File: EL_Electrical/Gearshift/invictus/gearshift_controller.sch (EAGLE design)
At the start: 70 parts, among them IC1 MCP2562-E_SN, IC2 MCP2515-I_SO, Q1 BSS138, Q10 BSS138, Q2 BSS138, Q3 BSS138, Q4 BSS138, Q5 BSS138, Q6 BSS138, Q8 BSS138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

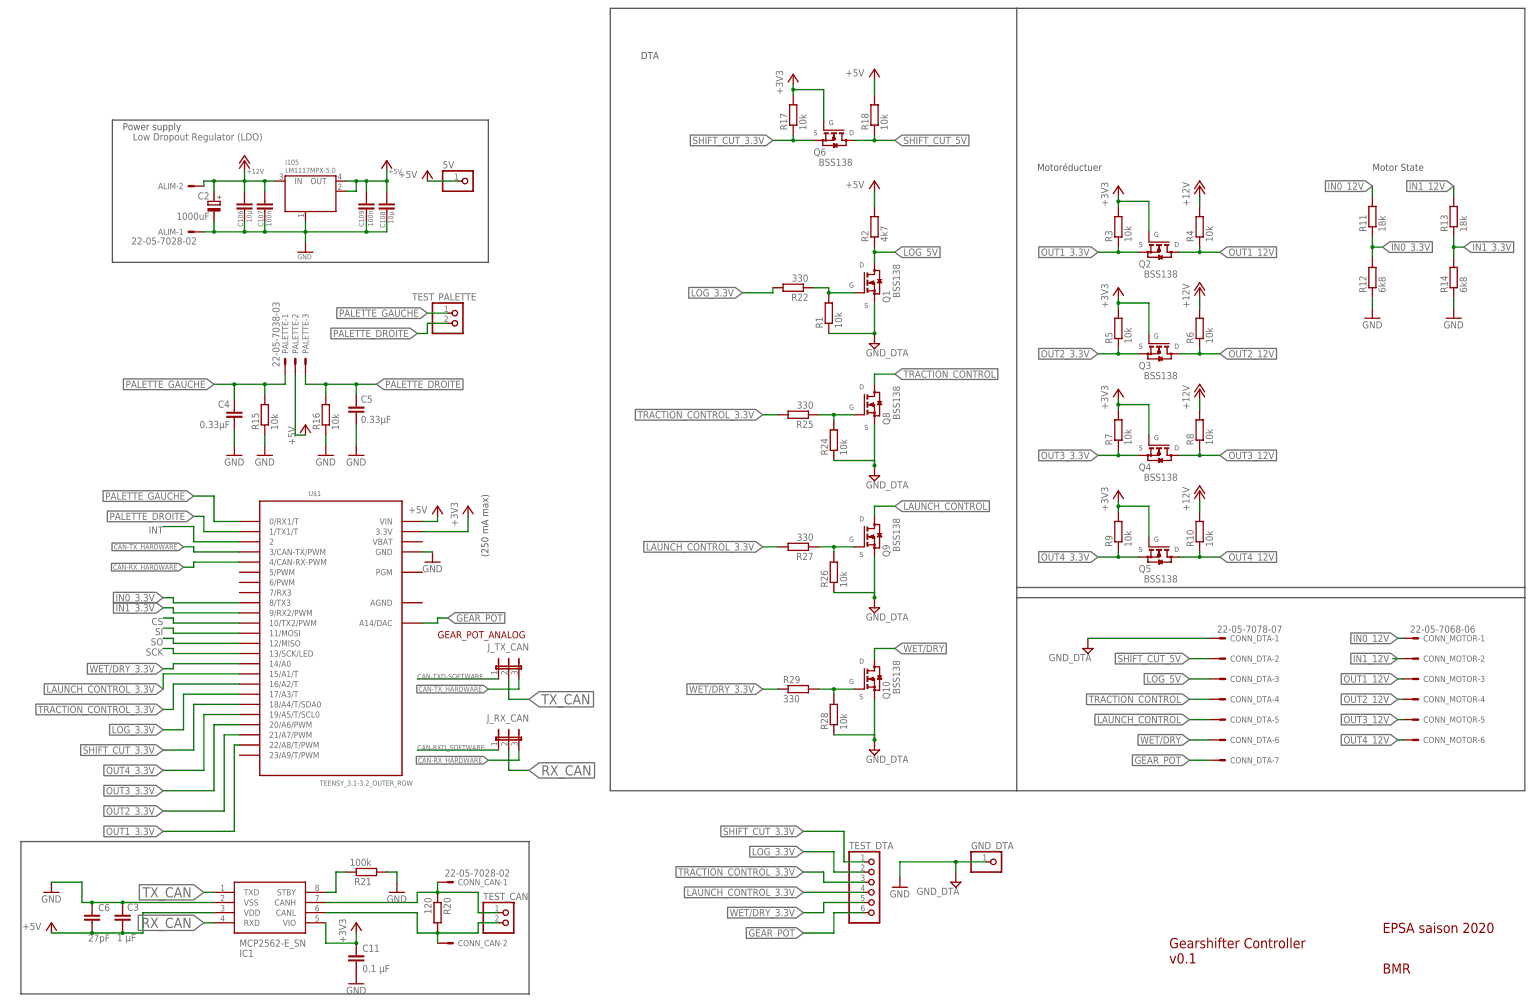
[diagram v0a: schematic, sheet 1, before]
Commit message: Add neutral sensor connector (to use with Teensy's pull-up resistors), delete uselless dta test pins
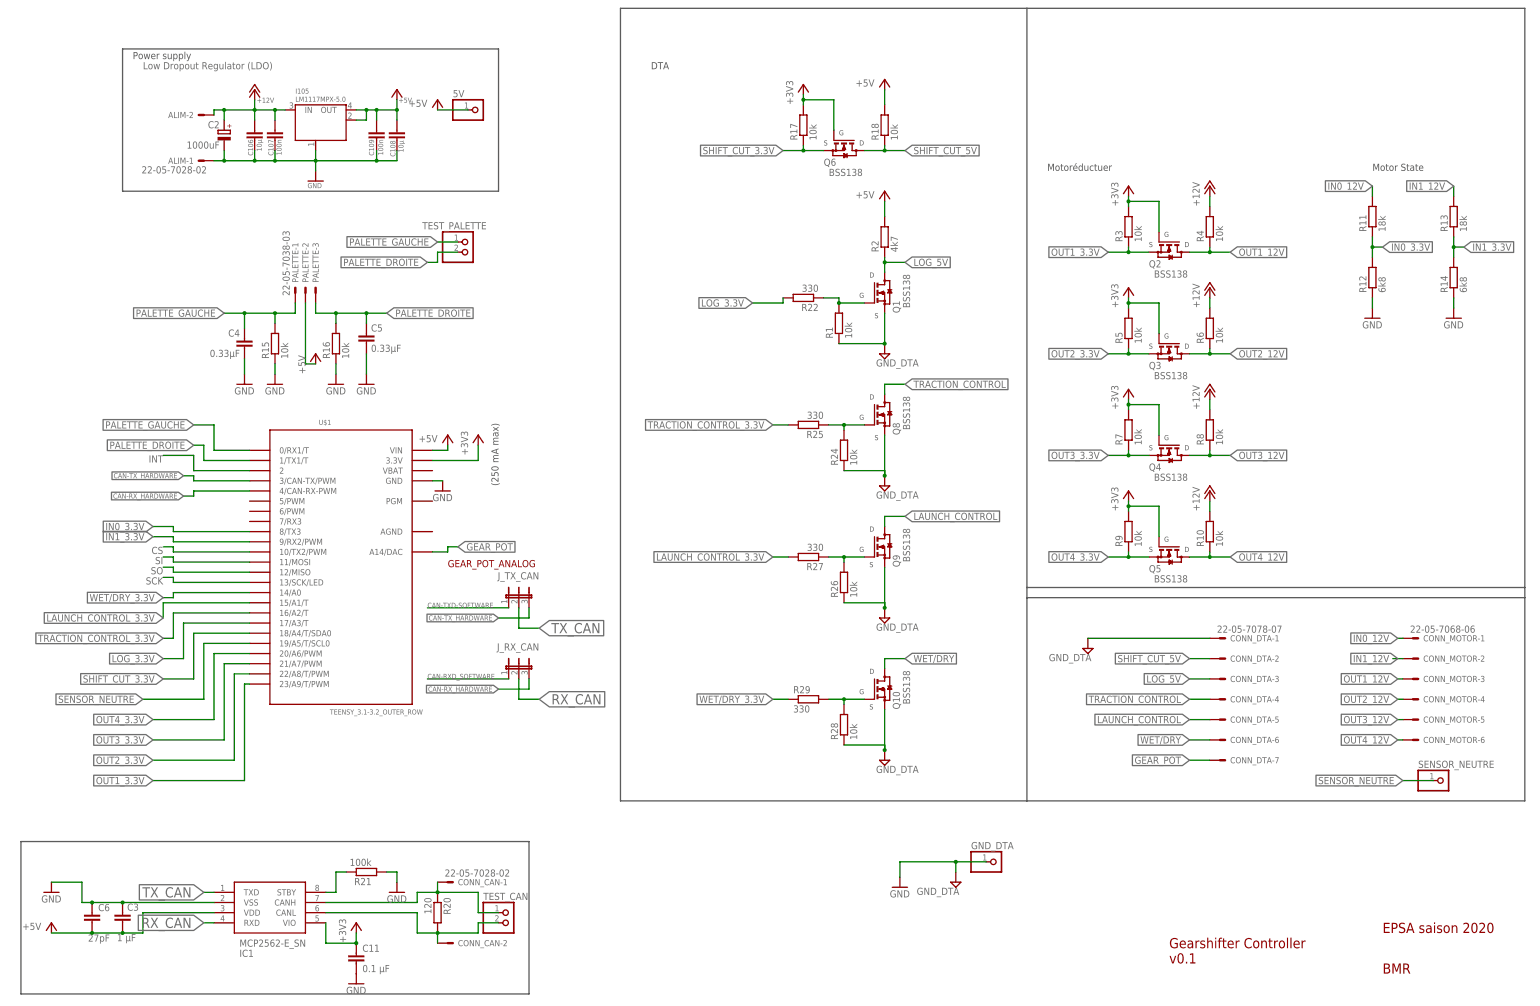
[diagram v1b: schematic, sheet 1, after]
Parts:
- removed TEST_DTA: (no value), test_pin_DTA:PINHD-1X6
- added SENSOR_NEUTRE: (no value), pinhead:PINHD-1X1
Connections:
- new net SENSOR_NEUTRE: SENSOR_NEUTRE.1, U$1.19/A5/T/SCL0
- net GEAR_POT: no longer TEST_DTA.6
- net LAUNCH_CONTROL_3.3V: no longer TEST_DTA.4
- net LOG_3.3V: no longer TEST_DTA.2
- net OUT1_3.3V: now also U$1.23/A9/T/PWM; no longer U$1.22/A8/T/PWM
- net OUT2_3.3V: now also U$1.22/A8/T/PWM; no longer U$1.21/A7/PWM
- net OUT3_3.3V: now also U$1.21/A7/PWM; no longer U$1.20/A6/PWM
- net OUT4_3.3V: now also U$1.20/A6/PWM; no longer U$1.19/A5/T/SCL0
- net SHIFT_CUT_3.3V: no longer TEST_DTA.1
- net TRACTION_CONTROL_3.3V: no longer TEST_DTA.3
- net WET/DRY_3.3V: no longer TEST_DTA.5
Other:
- moved on the sheet: 5V, ALIM-1, ALIM-2, C106, C107, C108, C109, C2, C4, C5, I105, J_RX_CAN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

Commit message: Change connector footprint, LDO regulator (DC linear voltage regulator) position and reduce the size for Gearshift Controller pcb Reduce 1mm for Dashboard Controller pcb
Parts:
- removed TEST_CAN: (no value), test_pin_DTA:PINHD-1X2
- ALIM: value 22-05-7028-02 -> 22-27-2021-02; device EP_molex_6410_7395:22-05-7028-02 -> con-molex:22-27-2021-02
- CONN_CAN: value 22-05-7028-02 -> 22-27-2021-02; device con-molex:22-05-7028-02 -> con-molex:22-27-2021-02
- CONN_DTA: value 22-05-7078-07 -> 22-27-2071-07; device con-molex:22-05-7078-07 -> con-molex:22-27-2071-07
- CONN_MOTOR: value 22-05-7068-06 -> 22-27-2061-06; device con-molex:22-05-7068-06 -> con-molex:22-27-2061-06
- PALETTE: value 22-05-7038-03 -> 22-27-2031-03; device EP_molex_6410_7395:22-05-7038-03 -> con-molex:22-27-2031-03
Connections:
- net N$4: no longer TEST_CAN.1
- net N$6: no longer TEST_CAN.2
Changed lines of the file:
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@@
 <part name="GND5" library="supply1" deviceset="GND" device=""/>
 <part name="GND9" library="supply1" deviceset="GND" device=""/>
-<part name="PALETTE" library="EP_molex_6410_7395" deviceset="22-?-03" device="05-7038"/>
+<part name="PALETTE" library="con-molex" library_urn="urn:adsk.eagle:library:165" deviceset="22-?-03" device="27-2031" package3d_urn="urn:adsk.eagle:package:8078647/1"/>
 <part name="P+9" library="supply1" library_urn="urn:adsk.eagle:library:371" deviceset="+5V" device=""/>
 <part name="R15" library="rcl" library_urn="urn:adsk.eagle:library:334" deviceset="R-EU_" device="R0805" package3d_urn="urn:adsk.eagle:package:23553/2" value="10k"/>
@@
 <part name="FRAME2" library="frames" library_urn="urn:adsk.eagle:library:229" deviceset="A4L-LOC" device=""/>
 <part name="+3V7" library="supply1" library_urn="urn:adsk.eagle:library:371" deviceset="+3V3" device=""/>
-<part name="CONN_CAN" library="con-molex" library_urn="urn:adsk.eagle:library:165" deviceset="22-?-02" device="05-7028" package3d_urn="urn:adsk.eagle:package:8078644/1"/>
+<part name="CONN_CAN" library="con-molex" library_urn="urn:adsk.eagle:library:165" deviceset="22-?-02" device="27-2021" package3d_urn="urn:adsk.eagle:package:8078645/1" value="22-27-2021-02"/>
 <part name="R20" library="rcl" library_urn="urn:adsk.eagle:library:334" deviceset="R-EU_" device="R0805" package3d_urn="urn:adsk.eagle:package:23553/2" value="120 "/>
 <part name="GND14" library="supply1" deviceset="GND" device=""/>
@@
 <part name="R28" library="rcl" library_urn="urn:adsk.eagle:library:334" deviceset="R-EU_" device="R0805" package3d_urn="urn:adsk.eagle:package:23553/2" value="10k"/>
 <part name="R29" library="rcl" library_urn="urn:adsk.eagle:library:334" deviceset="R-EU_" device="R0805" package3d_urn="urn:adsk.eagle:package:23553/2" value="330"/>
-<part name="ALIM" library="EP_molex_6410_7395" deviceset="22-?-02" device="05-7028"/>
-<part name="CONN_MOTOR" library="con-molex" library_urn="urn:adsk.eagle:library:165" deviceset="22-?-06" device="05-7068" package3d_urn="urn:adsk.eagle:package:8078652/1"/>
+<part name="ALIM" library="con-molex" library_urn="urn:adsk.eagle:library:165" deviceset="22-?-02" device="27-2021" package3d_urn="urn:adsk.eagle:package:8078645/1"/>
+<part name="CONN_MOTOR" library="con-molex" library_urn="urn:adsk.eagle:library:165" deviceset="22-?-06" device="27-2061" package3d_urn="urn:adsk.eagle:package:8078653/1" value="22-27-2061-06"/>
 <part name="SUPPLY1" library="supply2" library_urn="urn:adsk.eagle:library:372" deviceset="GND1" device="" value="GND_DTA"/>
 <part name="SUPPLY2" library="supply2" library_urn="urn:adsk.eagle:library:372" deviceset="GND1" device="" value="GND_DTA"/>
@@
 <part name="SUPPLY4" library="supply2" library_urn="urn:adsk.eagle:library:372" deviceset="GND1" device="" value="GND_DTA"/>
 <part name="SUPPLY5" library="supply2" library_urn="urn:adsk.eagle:library:372" deviceset="GND1" device="" value="GND_DTA"/>
-<part name="CONN_DTA" library="con-molex" library_urn="urn:adsk.eagle:library:165" deviceset="22-?-07" device="05-7078" package3d_urn="urn:adsk.eagle:package:8078654/1"/>
+<part name="CONN_DTA" library="con-molex" library_urn="urn:adsk.eagle:library:165" deviceset="22-?-07" device="27-2071" package3d_urn="urn:adsk.eagle:package:8078655/1" value="22-27-2071-07"/>
 <part name="R23" library="rcl" library_urn="urn:adsk.eagle:library:334" deviceset="R-EU_" device="R0805" package3d_urn="urn:adsk.eagle:package:23553/2" value="1k"/>
 <part name="+3V1" library="supply1" library_urn="urn:adsk.eagle:library:371" deviceset="+3V3" device=""/>
@@
 <part name="SUPPLY6" library="supply2" library_urn="urn:adsk.eagle:library:372" deviceset="GND1" device="" value="GND_DTA"/>
 <part name="GND2" library="supply1" deviceset="GND" device=""/>
-<part name="TEST_CAN" library="test_pin_DTA" deviceset="PINHD-1X2" device="" package3d_urn="urn:adsk.eagle:package:22435/2"/>
 <part name="TEST_PALETTE" library="test_pin_DTA" deviceset="PINHD-1X2" device="" package3d_urn="urn:adsk.eagle:package:22435/2"/>
 <part name="C2" library="rcl" library_urn="urn:adsk.eagle:library:334" deviceset="CPOL-EU" device="E25-10AXIAL" package3d_urn="urn:adsk.eagle:package:23352/1" value="1000uF"/>
@@
 <attribute name="VALUE" x="222.25" y="29.21" size="1.778" layer="96"/>
 </instance>
-<instance part="TEST_CAN" gate="G$1" x="127" y="22.86" smashed="yes">
-<attribute name="NAME" x="120.65" y="28.575" size="1.778" layer="95"/>
-<attribute name="VALUE" x="120.65" y="17.78" size="1.778" layer="96"/>
-</instance>
 <instance part="TEST_PALETTE" gate="G$1" x="116.84" y="190.5" smashed="yes">
 <attribute name="NAME" x="105.41" y="196.215" size="1.778" layer="95"/>
@@
 <wire x1="109.22" y1="30.48" x2="109.22" y2="33.02" width="0.1524" layer="91"/>
 <junction x="109.22" y="30.48"/>
-<wire x1="109.22" y1="30.48" x2="119.38" y2="30.48" width="0.1524" layer="91"/>
-<wire x1="119.38" y1="30.48" x2="119.38" y2="25.4" width="0.1524" layer="91"/>
-<pinref part="TEST_CAN" gate="G$1" pin="1"/>
-<wire x1="119.38" y1="25.4" x2="124.46" y2="25.4" width="0.1524" layer="91"/>
 </segment>
 </net>
@@
 <wire x1="109.22" y1="17.78" x2="109.22" y2="20.32" width="0.1524" layer="91"/>
 <junction x="109.22" y="20.32"/>
-<pinref part="TEST_CAN" gate="G$1" pin="2"/>
-<wire x1="124.46" y1="22.86" x2="119.38" y2="22.86" width="0.1524" layer="91"/>
-<wire x1="119.38" y1="22.86" x2="119.38" y2="20.32" width="0.1524" layer="91"/>
-<wire x1="119.38" y1="20.32" x2="109.22" y2="20.32" width="0.1524" layer="91"/>
-</segment>
-</net>
+</segment>
+</net>

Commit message: Update holes and text
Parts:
- renumbered ALIM to POWER
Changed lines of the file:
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@@
 <part name="R28" library="rcl" library_urn="urn:adsk.eagle:library:334" deviceset="R-EU_" device="R0805" package3d_urn="urn:adsk.eagle:package:23553/2" value="10k"/>
 <part name="R29" library="rcl" library_urn="urn:adsk.eagle:library:334" deviceset="R-EU_" device="R0805" package3d_urn="urn:adsk.eagle:package:23553/2" value="330"/>
-<part name="ALIM" library="con-molex" library_urn="urn:adsk.eagle:library:165" deviceset="22-?-02" device="27-2021" package3d_urn="urn:adsk.eagle:package:8078645/1"/>
+<part name="POWER" library="con-molex" library_urn="urn:adsk.eagle:library:165" deviceset="22-?-02" device="27-2021" package3d_urn="urn:adsk.eagle:package:8078645/1"/>
 <part name="CONN_MOTOR" library="con-molex" library_urn="urn:adsk.eagle:library:165" deviceset="22-?-06" device="27-2061" package3d_urn="urn:adsk.eagle:package:8078653/1" value="22-27-2061-06"/>
 <part name="SUPPLY1" library="supply2" library_urn="urn:adsk.eagle:library:372" deviceset="GND1" device="" value="GND_DTA"/>
@@
 <attribute name="VALUE" x="198.12" y="75.438" size="1.778" layer="96"/>
 </instance>
-<instance part="ALIM" gate="-1" x="50.8" y="213.36" smashed="yes" rot="R180">
+<instance part="POWER" gate="-1" x="50.8" y="213.36" smashed="yes" rot="R180">
 <attribute name="NAME" x="48.26" y="214.122" size="1.524" layer="95" rot="R180"/>
 <attribute name="VALUE" x="51.562" y="211.963" size="1.778" layer="96" rot="R180"/>
 </instance>
-<instance part="ALIM" gate="-2" x="50.8" y="224.79" smashed="yes" rot="R180">
+<instance part="POWER" gate="-2" x="50.8" y="224.79" smashed="yes" rot="R180">
 <attribute name="NAME" x="48.26" y="225.552" size="1.524" layer="95" rot="R180"/>
 </instance>
@@
 <junction x="63.5" y="226.06"/>
 <pinref part="P+11" gate="1" pin="+12V"/>
-<pinref part="ALIM" gate="-2" pin="S"/>
+<pinref part="POWER" gate="-2" pin="S"/>
 <wire x1="53.34" y1="224.79" x2="53.34" y2="226.06" width="0.1524" layer="91"/>
 <wire x1="53.34" y1="226.06" x2="55.88" y2="226.06" width="0.1524" layer="91"/>
@@
 <pinref part="C108" gate="G$1" pin="2"/>
 <pinref part="C106" gate="G$1" pin="2"/>
-<pinref part="ALIM" gate="-1" pin="S"/>
+<pinref part="POWER" gate="-1" pin="S"/>
 <wire x1="63.5" y1="213.36" x2="55.88" y2="213.36" width="0.1524" layer="91"/>
 <junction x="63.5" y="213.36"/>
